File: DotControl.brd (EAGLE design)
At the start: 30.7 x 65 mm, 24 parts, among them CN1 1X4-BIG, J3 USB-MICROB, SW2 Previous, SW5 Previous, SW6 Next, SW8 Ok, U1 ATMEGA328P-MU-QFN32

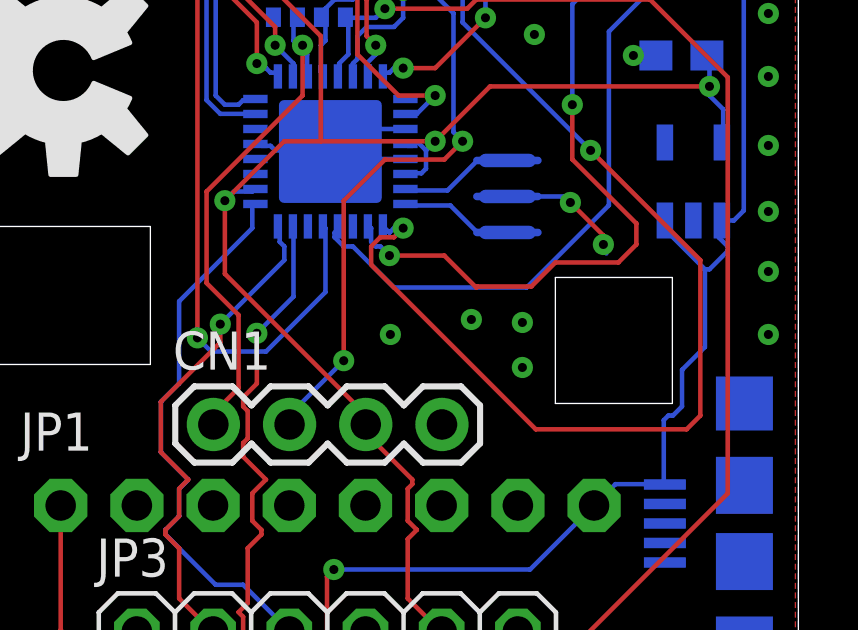
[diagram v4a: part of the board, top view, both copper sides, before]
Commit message: Add TMP112 temperature sensor
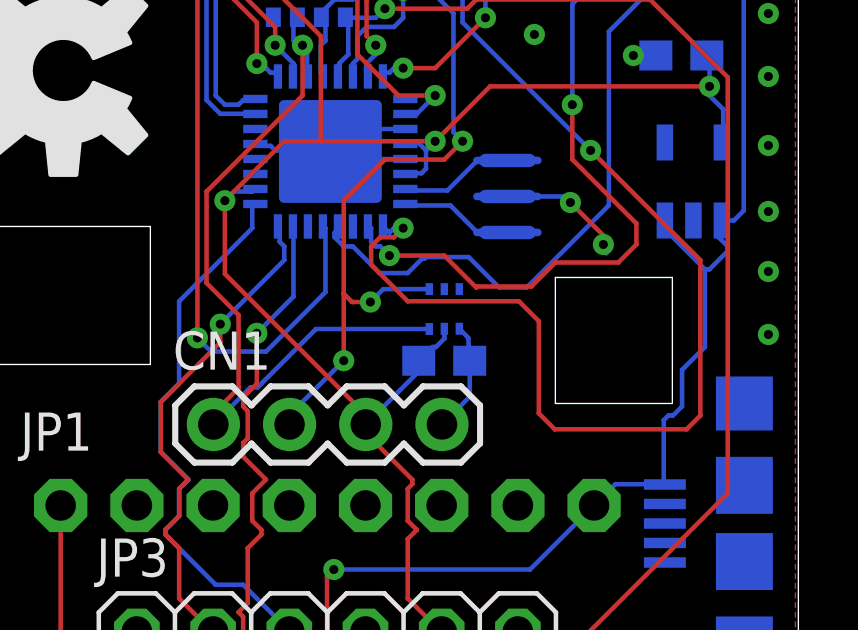
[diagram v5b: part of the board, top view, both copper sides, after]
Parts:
- added C3: 0.1uF, resistor:C0603
- added U2: TMP102, SparkFun:SOT563
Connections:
- new net INT_MULTIPLE: U2.3
- net +3V3: now also C3.1, U2.5
- net GND: now also C3.2, U2.2, U2.4
- net SCL: now also U2.1
- net SDA: now also U2.6
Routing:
- net SDA: track 17.2 -> 25.7 mm
- net +3V3: track 118.4 -> 122.8 mm
- net GND: track 12.4 -> 16.1 mm, vias 97 -> 93
- net SCL: track 25.2 -> 28.4 mm, vias 2 -> 3
- net RSDI: track 50.8 -> 52.6 mm
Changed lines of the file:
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@@
 <element name="R1" library="resistor" package="R0603" value="" x="27.6352" y="60.5282" rot="MR270"/>
 <element name="LED2" library="SparkFun" package="LED-0603" value="" x="27.4828" y="60.6044" rot="R180"/>
+<element name="U2" library="SparkFun" package="SOT563" value="TMP102" x="18.8976" y="12.8524" rot="MR180"/>
+<element name="C3" library="resistor" package="C0603" value="0.1uF" x="18.8976" y="11.1252" rot="MR180"/>
 </elements>
 <signals>
@@
 <wire x1="23.1" y1="16.4" x2="22.9" y2="16.6" width="0.1524" layer="16"/>
 <wire x1="22.9" y1="16.6" x2="21" y2="16.6" width="0.1524" layer="16"/>
-<via x="19.8" y="12.5" extent="1-16" drill="0.3"/>
-<via x="21.5" y="10.9" extent="1-16" drill="0.3"/>
-<via x="21.5" y="12.4" extent="1-16" drill="0.3"/>
-<via x="17.1" y="12" extent="1-16" drill="0.3"/>
 <contactref element="LED2" pad="C"/>
+<contactref element="U2" pad="2"/>
+<contactref element="C3" pad="2"/>
+<contactref element="U2" pad="4"/>
+<wire x1="19.3976" y1="12.1924" x2="19.6968" y2="11.8876" width="0.1524" layer="16"/>
+<wire x1="19.6968" y1="11.8876" x2="19.7476" y2="11.1252" width="0.1524" layer="16"/>
+<wire x1="19.7476" y1="11.1252" x2="19.7476" y2="9.9276" width="0.1524" layer="16"/>
+<wire x1="19.7476" y1="9.9276" x2="18.82" y2="9" width="0.1524" layer="16"/>
 </signal>
 <signal name="SCK">
@@
 <wire x1="11.2776" y1="9.144" x2="11.2" y2="9" width="0.1524" layer="1"/>
 <via x="14.1732" y="21.6408" extent="1-16" drill="0.3"/>
+<contactref element="U2" pad="6"/>
+<wire x1="18.3976" y1="12.1824" x2="14.6208" y2="12.1824" width="0.1524" layer="16"/>
+<wire x1="14.6208" y1="12.1824" x2="12.6746" y2="10.2362" width="0.1524" layer="16"/>
+<wire x1="12.6746" y1="10.2362" x2="12.4362" y2="10.2362" width="0.1524" layer="16"/>
+<wire x1="12.4362" y1="10.2362" x2="11.2" y2="9" width="0.1524" layer="16"/>
 </signal>
 <signal name="SCL">
@@
 <wire x1="16.9164" y1="17.8308" x2="18.8976" y2="17.8308" width="0.1524" layer="1"/>
 <wire x1="15.5448" y1="16.4592" x2="16.9164" y2="17.8308" width="0.1524" layer="1"/>
-<wire x1="15.5448" y1="11.1252" x2="15.5448" y2="16.4592" width="0.1524" layer="1"/>
+<wire x1="15.5448" y1="11.1252" x2="15.5448" y2="13.3604" width="0.1524" layer="1"/>
+<wire x1="15.5448" y1="13.3604" x2="15.5448" y2="16.4592" width="0.1524" layer="1"/>
 <wire x1="13.8684" y1="9.4488" x2="15.5448" y2="11.1252" width="0.1524" layer="16"/>
 <wire x1="13.8684" y1="9.144" x2="13.8684" y2="9.4488" width="0.1524" layer="16"/>
@@
 <via x="19.5072" y="18.4404" extent="1-16" drill="0.3"/>
 <via x="15.5448" y="11.1252" extent="1-16" drill="0.3"/>
+<contactref element="U2" pad="1"/>
+<wire x1="18.3976" y1="13.5124" x2="16.8652" y2="13.5124" width="0.1524" layer="16"/>
+<wire x1="16.8652" y1="13.5124" x2="16.4338" y2="13.081" width="0.1524" layer="16"/>
+<via x="16.4338" y="13.081" extent="1-16" drill="0.3"/>
+<wire x1="16.4338" y1="13.081" x2="15.8242" y2="13.081" width="0.1524" layer="1"/>
+<wire x1="15.8242" y1="13.081" x2="15.5448" y2="13.3604" width="0.1524" layer="1"/>
 </signal>
 <signal name="RST">
@@
 <via x="27.7368" y="20.2692" extent="1-16" drill="0.3"/>
 <via x="13.1064" y="24.6888" extent="1-16" drill="0.3"/>
+<contactref element="C3" pad="1"/>
+<contactref element="U2" pad="5"/>
+<wire x1="18.8976" y1="12.1924" x2="18.8976" y2="11.8618" width="0.1524" layer="16"/>
+<wire x1="18.8976" y1="11.8618" x2="18.6182" y2="11.5824" width="0.1524" layer="16"/>
+<wire x1="18.6182" y1="11.5824" x2="18.5048" y2="11.5824" width="0.1524" layer="16"/>
+<wire x1="18.5048" y1="11.5824" x2="18.0476" y2="11.1252" width="0.1524" layer="16"/>
+<wire x1="18.0476" y1="11.1252" x2="18.0476" y2="10.7676" width="0.1524" layer="16"/>
+<wire x1="18.0476" y1="10.7676" x2="16.28" y2="9" width="0.1524" layer="16"/>
 <wire x1="14.8" y1="23.825" x2="16.7" y2="26.908" width="0" layer="19" extent="16-16"/>
 </signal>
@@
 <wire x1="24.384" y1="16.3068" x2="24.384" y2="22.098" width="0.1524" layer="16"/>
 <wire x1="21.6408" y1="13.5636" x2="24.384" y2="16.3068" width="0.1524" layer="16"/>
-<wire x1="17.2212" y1="13.5636" x2="21.6408" y2="13.5636" width="0.1524" layer="16"/>
-<wire x1="15.8496" y1="14.9352" x2="17.2212" y2="13.5636" width="0.1524" layer="16"/>
 <wire x1="15.5448" y1="14.9352" x2="15.8496" y2="14.9352" width="0.1524" layer="16"/>
 <wire x1="15.24" y1="15.24" x2="15.5448" y2="14.9352" width="0.1524" layer="16"/>
@@
 <via x="14.478" y="54.102" extent="1-16" drill="0.3"/>
 <via x="26.0604" y="23.7744" extent="1-16" drill="0.3"/>
+<wire x1="15.8496" y1="14.9352" x2="16.7386" y2="14.0462" width="0.1524" layer="16"/>
+<wire x1="16.7386" y1="14.0462" x2="17.6784" y2="14.0462" width="0.1524" layer="16"/>
+<wire x1="17.6784" y1="14.0462" x2="18.161" y2="14.5288" width="0.1524" layer="16"/>
+<wire x1="18.161" y1="14.5288" x2="18.2372" y2="14.5288" width="0.1524" layer="16"/>
+<wire x1="18.2372" y1="14.5288" x2="18.288" y2="14.5796" width="0.1524" layer="16"/>
+<wire x1="18.288" y1="14.5796" x2="19.7104" y2="14.5796" width="0.1524" layer="16"/>
+<wire x1="19.7104" y1="14.5796" x2="20.7264" y2="13.5636" width="0.1524" layer="16"/>
+<wire x1="20.7264" y1="13.5636" x2="21.6408" y2="13.5636" width="0.1524" layer="16"/>
 </signal>
 <signal name="LIGHT_SENSE">
@@
 <wire x1="16.4592" y1="14.9352" x2="16.764" y2="15.24" width="0.1524" layer="1"/>
 <wire x1="16.4592" y1="14.3256" x2="16.4592" y2="14.9352" width="0.1524" layer="1"/>
-<wire x1="21.9456" y1="8.8392" x2="16.4592" y2="14.3256" width="0.1524" layer="1"/>
-<wire x1="26.9748" y1="8.8392" x2="21.9456" y2="8.8392" width="0.1524" layer="1"/>
 <wire x1="27.432" y1="9.2964" x2="26.9748" y2="8.8392" width="0.1524" layer="1"/>
 <wire x1="27.432" y1="14.478" x2="27.432" y2="9.2964" width="0.1524" layer="1"/>
@@
 <via x="17.526" y="15.5448" extent="1-16" drill="0.3"/>
 <via x="23.7744" y="18.1356" extent="1-16" drill="0.3"/>
+<wire x1="16.4592" y1="14.3256" x2="17.6784" y2="13.1064" width="0.1524" layer="1"/>
+<wire x1="17.6784" y1="13.1064" x2="21.3868" y2="13.1064" width="0.1524" layer="1"/>
+<wire x1="21.3868" y1="13.1064" x2="22.0472" y2="12.446" width="0.1524" layer="1"/>
+<wire x1="22.0472" y1="12.446" x2="22.0472" y2="9.3726" width="0.1524" layer="1"/>
+<wire x1="22.0472" y1="9.3726" x2="22.5806" y2="8.8392" width="0.1524" layer="1"/>
+<wire x1="22.5806" y1="8.8392" x2="26.9748" y2="8.8392" width="0.1524" layer="1"/>
 </signal>
 <signal name="RSDO">
@@
 <wire x1="27.5962" y1="61.4172" x2="27.6352" y2="61.3782" width="0.1524" layer="16"/>
 </signal>
+<signal name="INT_MULTIPLE">
+<contactref element="U2" pad="3"/>
+</signal>
 </signals>

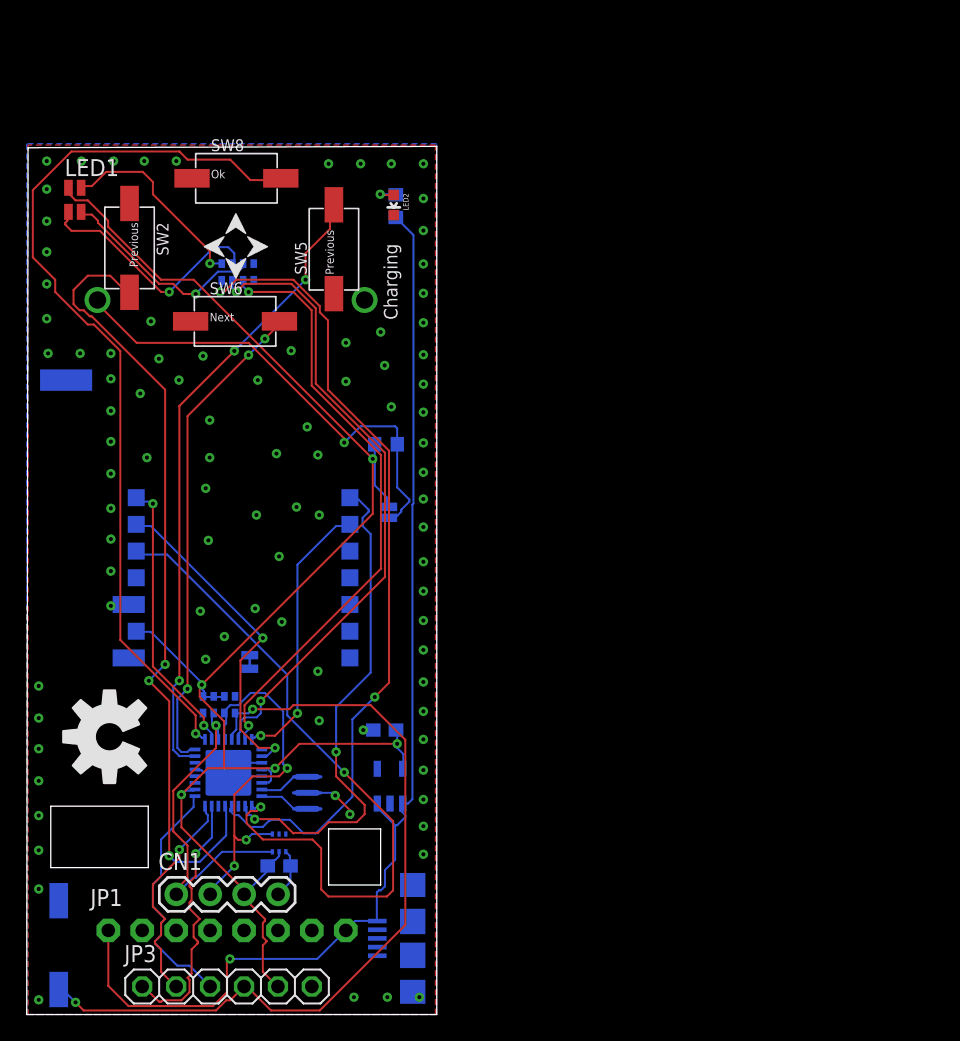
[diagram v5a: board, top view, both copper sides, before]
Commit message: Solidify GND plane
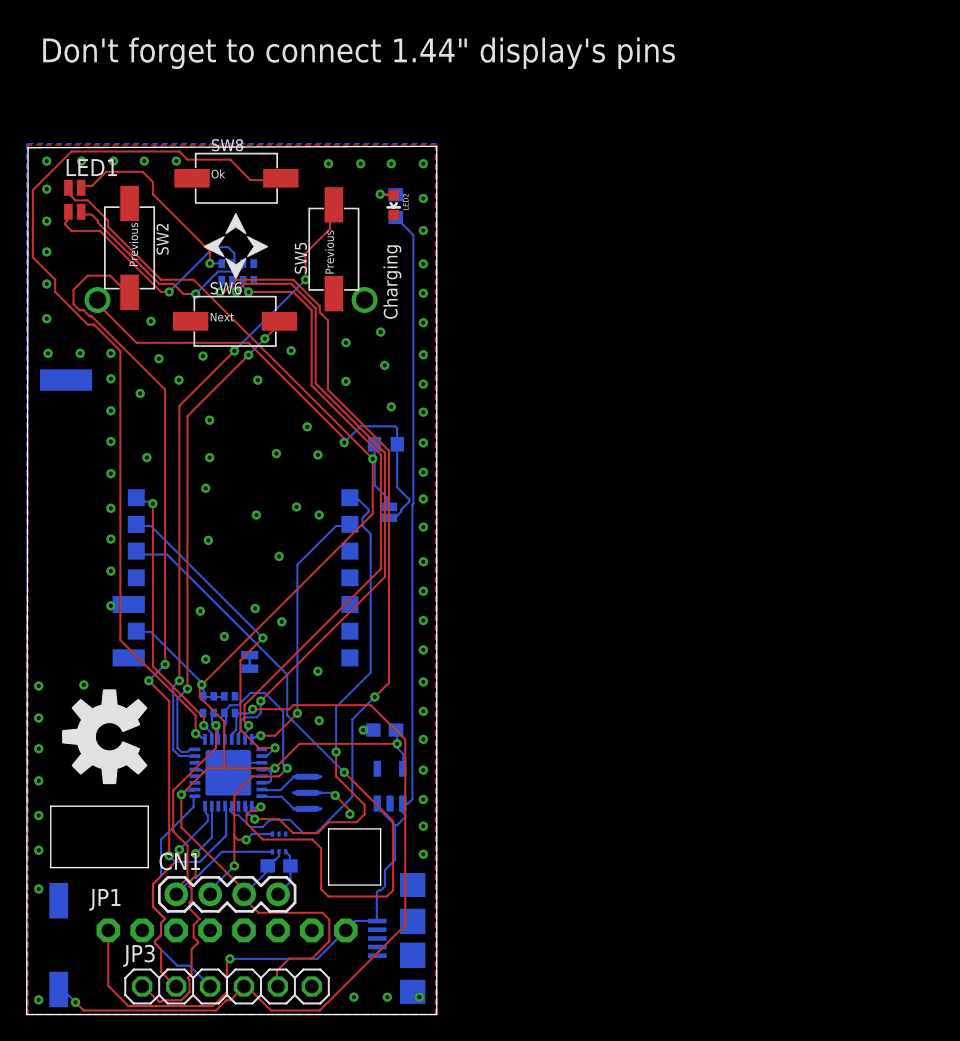
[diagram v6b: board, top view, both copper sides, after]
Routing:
- net +3V3: track 122.8 -> 129.8 mm
- net GND: vias 93 -> 94
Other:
- board text added: "Don't forget to connect 1.44" display's pins"
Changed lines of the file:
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@@
 <rectangle x1="15.6337" y1="59.9821" x2="15.6845" y2="60.0075" layer="21"/>
 <text x="27.7622" y="52.0192" size="1.016" layer="21" font="vector" rot="R90">Charging</text>
+<text x="1.016" y="71.2978" size="1.778" layer="21">Don't forget to connect 1.44" display's pins</text>
 </plain>
 <attributes>
@@
 <wire x1="19.7476" y1="11.1252" x2="19.7476" y2="9.9276" width="0.1524" layer="16"/>
 <wire x1="19.7476" y1="9.9276" x2="18.82" y2="9" width="0.1524" layer="16"/>
+<via x="4.2782" y="24.6762" extent="1-16" drill="0.3"/>
 </signal>
 <signal name="SCK">
@@
 <wire x1="20.4216" y1="20.2692" x2="27.7368" y2="20.2692" width="0.1524" layer="1"/>
 <wire x1="18.5928" y1="18.4404" x2="20.4216" y2="20.2692" width="0.1524" layer="1"/>
-<wire x1="17.6784" y1="3.2004" x2="18.7452" y2="2.1336" width="0.1524" layer="1"/>
-<wire x1="17.6784" y1="5.1816" x2="17.6784" y2="3.2004" width="0.1524" layer="1"/>
-<wire x1="17.9832" y1="5.4864" x2="17.6784" y2="5.1816" width="0.1524" layer="1"/>
-<wire x1="17.6784" y1="5.7912" x2="17.9832" y2="5.4864" width="0.1524" layer="1"/>
-<wire x1="17.6784" y1="6.858" x2="17.6784" y2="5.7912" width="0.1524" layer="1"/>
-<wire x1="17.8308" y1="7.0104" x2="17.6784" y2="6.858" width="0.1524" layer="1"/>
-<wire x1="17.8308" y1="7.1628" x2="17.8308" y2="7.0104" width="0.1524" layer="1"/>
-<wire x1="16.3068" y1="8.6868" x2="17.8308" y2="7.1628" width="0.1524" layer="1"/>
 <wire x1="16.3068" y1="8.9916" x2="16.3068" y2="8.6868" width="0.1524" layer="1"/>
 <wire x1="18.7452" y1="2.1336" x2="18.81" y2="2.1" width="0.1524" layer="1"/>
@@
 <wire x1="18.0476" y1="11.1252" x2="18.0476" y2="10.7676" width="0.1524" layer="16"/>
 <wire x1="18.0476" y1="10.7676" x2="16.28" y2="9" width="0.1524" layer="16"/>
+<wire x1="18.7452" y1="2.1336" x2="18.7452" y2="3.2766" width="0.1524" layer="1"/>
+<wire x1="18.7452" y1="3.2766" x2="19.6596" y2="4.191" width="0.1524" layer="1"/>
+<wire x1="19.6596" y1="4.191" x2="21.3614" y2="4.191" width="0.1524" layer="1"/>
+<wire x1="21.3614" y1="4.191" x2="22.6568" y2="5.4864" width="0.1524" layer="1"/>
+<wire x1="22.6568" y1="5.4864" x2="22.6568" y2="7.112" width="0.1524" layer="1"/>
+<wire x1="22.6568" y1="7.112" x2="22.1488" y2="7.62" width="0.1524" layer="1"/>
+<wire x1="22.1488" y1="7.62" x2="17.3482" y2="7.62" width="0.1524" layer="1"/>
+<wire x1="17.3482" y1="7.62" x2="16.28" y2="8.6882" width="0.1524" layer="1"/>
+<wire x1="16.28" y1="8.6882" x2="16.28" y2="9" width="0.1524" layer="1"/>
 <wire x1="14.8" y1="23.825" x2="16.7" y2="26.908" width="0" layer="19" extent="16-16"/>
 </signal>

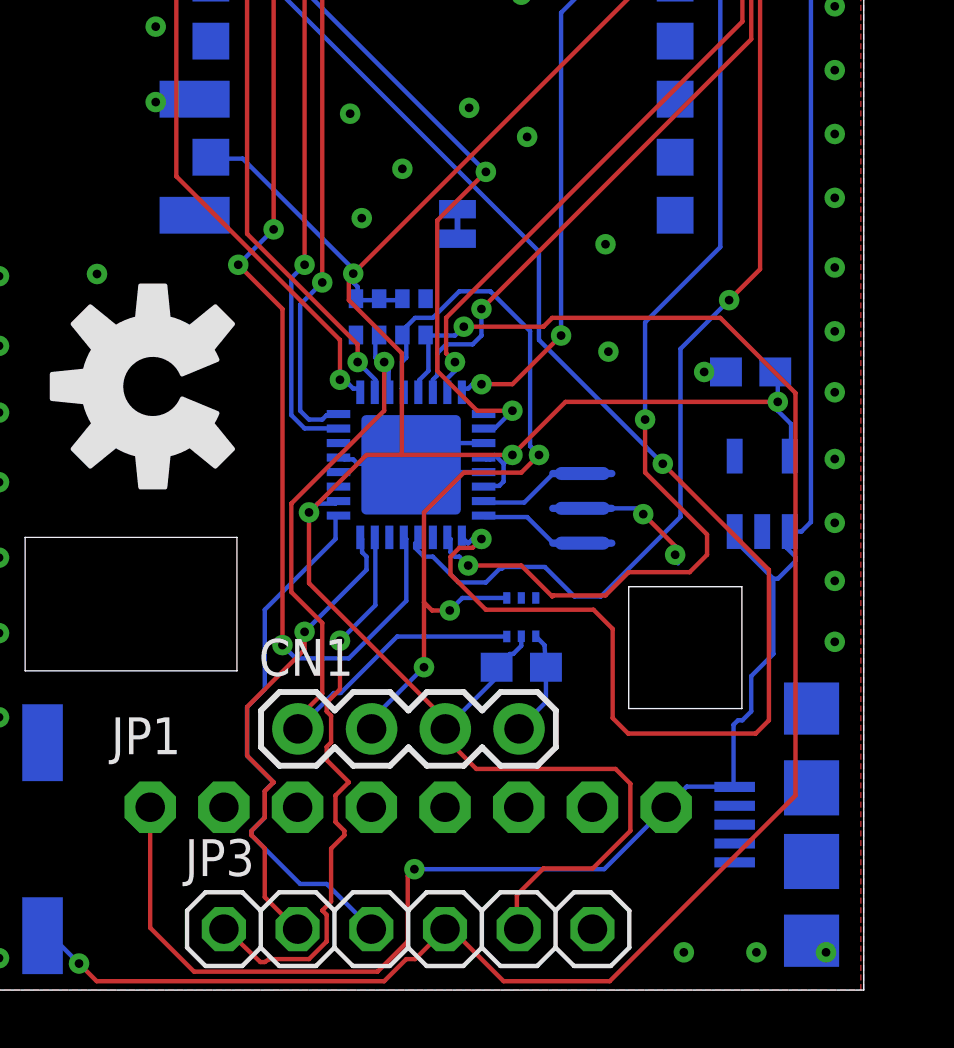
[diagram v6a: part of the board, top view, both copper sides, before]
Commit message: Add connections for 128x128
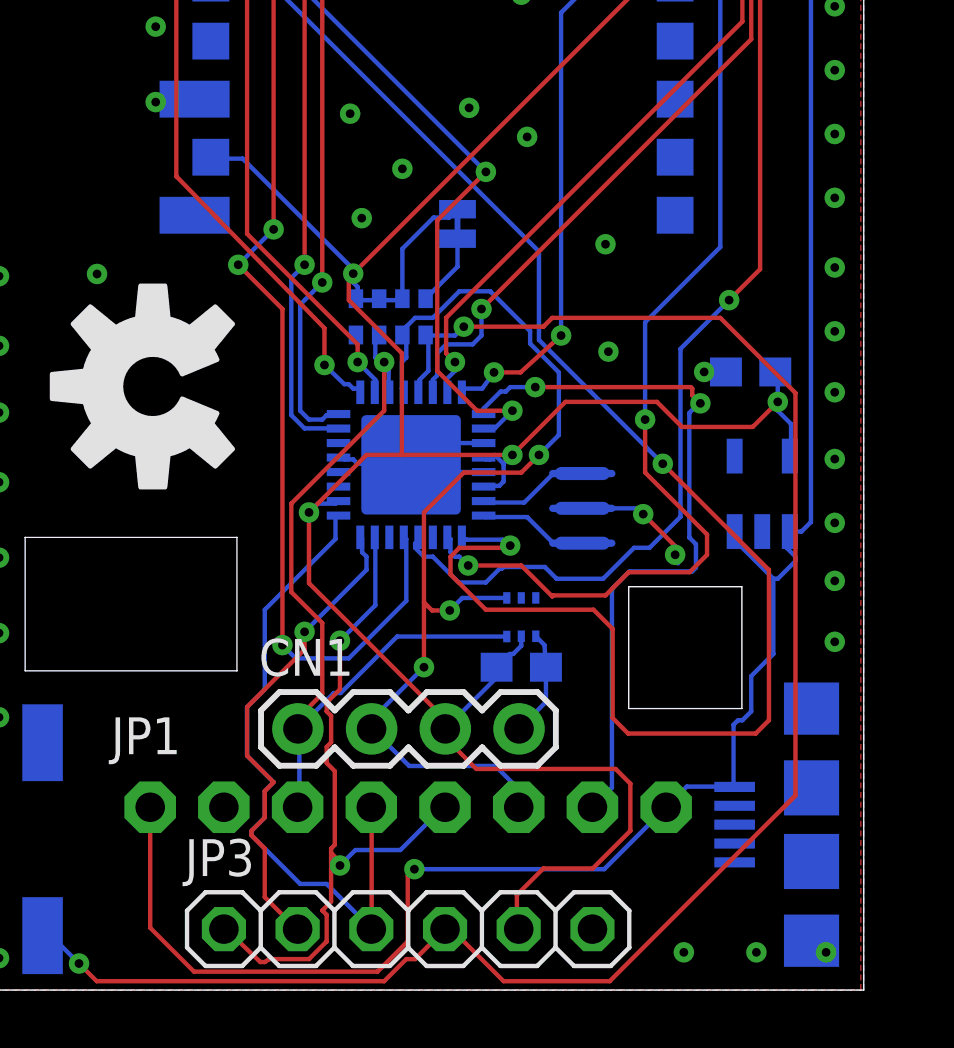
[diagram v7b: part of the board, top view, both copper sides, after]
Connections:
- removed net DISPLAY_SCK: JP1.7
- net PUSH: now also JP1.7
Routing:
- net PUSH: track 0.00 -> 25.3 mm, vias 0 -> 2
- net N$5: track 0.00 -> 6.60 mm
- net N$7: track 0.00 -> 5.05 mm, vias 0 -> 1
- net +3V3: track 129.8 -> 134.7 mm
- net N$4: track 0.00 -> 4.19 mm
- net N$11: track 0.00 -> 2.77 mm
- net N$2: track 0.00 -> 2.52 mm
- net RSDI: track 52.6 -> 54.4 mm
- net MOSI: track 20.1 -> 19.4 mm
- net SCL: track 28.4 -> 28.9 mm
- net LED: track 61.5 -> 61.0 mm
